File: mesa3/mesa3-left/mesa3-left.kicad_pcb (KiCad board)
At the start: 2 copper layers, 214 x 111 mm, 55 parts, among them J2 Tag-Connect TC2030

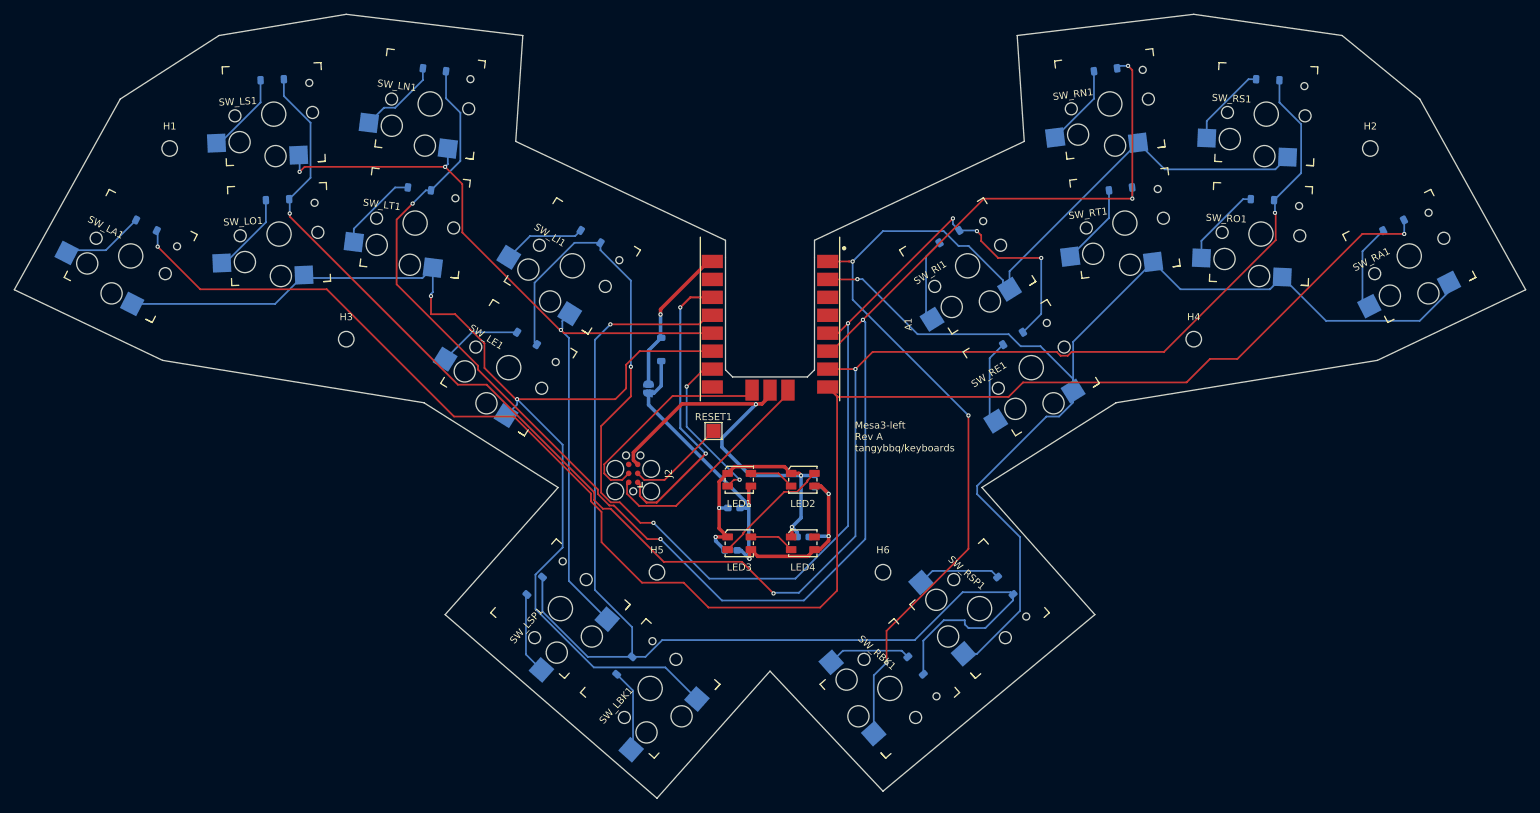
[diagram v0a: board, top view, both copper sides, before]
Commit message: Split the Mesa 3 into left and right halves
Each half now carries its own nine keys, its own outline and its own
routing. The left keeps the Tiny2040, the LEDs, the Tag-Connect and the
reset pad; the right is switches, diodes and the RJ-45 and nothing else,
with no power and no ground anywhere on it.

The two checks that mattered both hold. The RJ-45 pinout is identical at
both ends, so a straight-through cable is correct -- the pin order runs
opposite between the halves, which is what a part that cannot be mirrored
does, and does not matter since the nets match. And all eighteen keys
keep their exact mesa2 column and row, so one keymap still serves Rev B
and both halves.

Record the review findings as accepted rather than outstanding, and
correct LAYOUT.md: the unconnected GND that DRC reports is a false
positive. The symbol ties the module's ground pads into one net, so DRC
wants copper between them, but the module commons them internally and
the board does not need to.

Assisted-by: Claude:opus-5
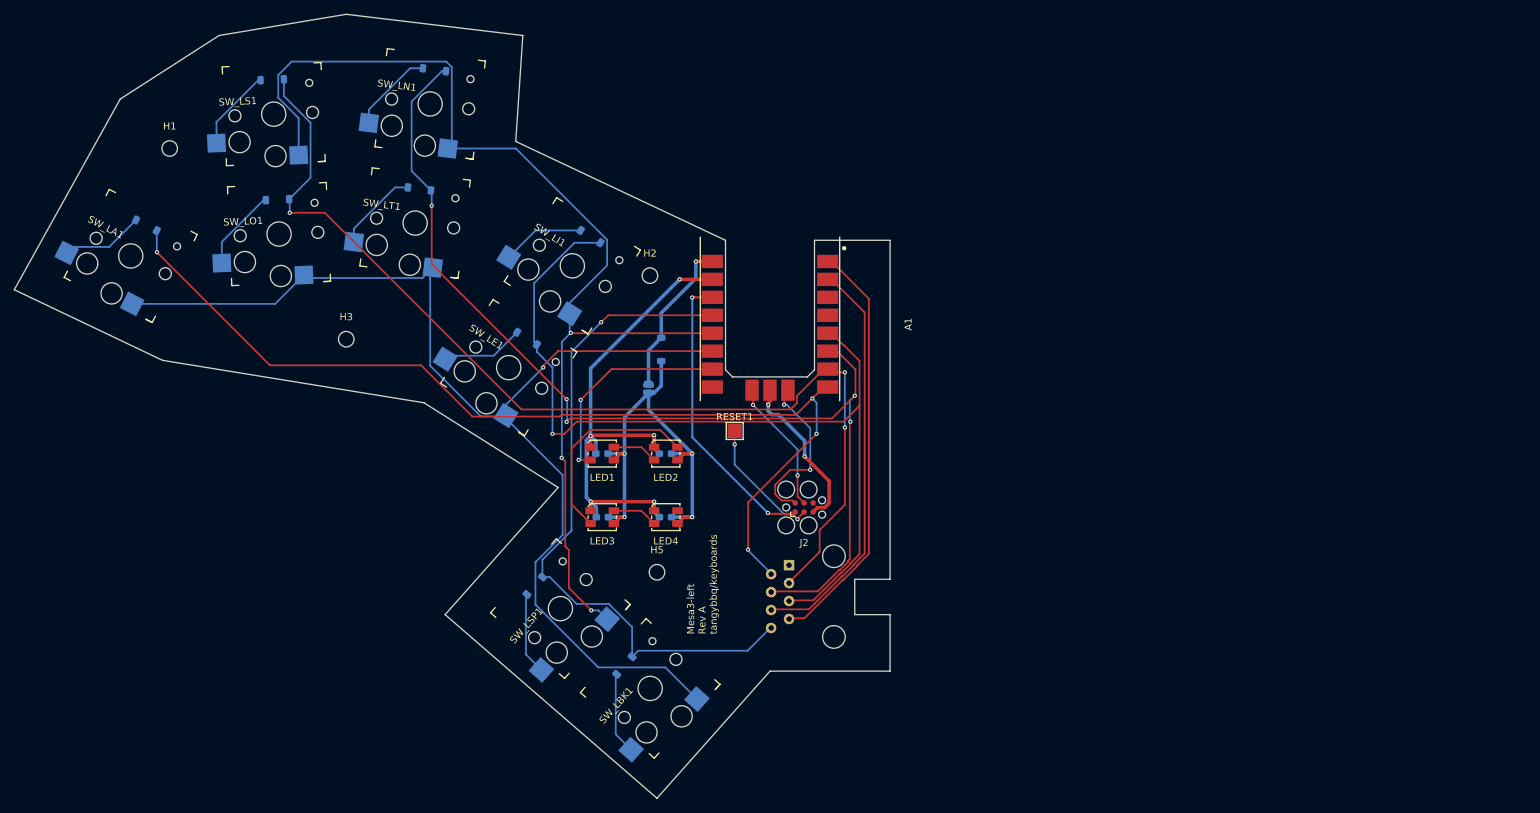
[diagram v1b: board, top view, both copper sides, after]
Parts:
- removed D_RA1, D_RBK1, D_RE1, D_RI1, D_RN1, D_RO1, D_RS1, D_RSP1, D_RT1: 1N4148W, Diode_SMD:D_SOD-123
- removed H4, H6: MountingHole, MountingHole:MountingHole_2.2mm_M2
- removed SW_RA1, SW_RBK1, SW_RE1, SW_RI1, SW_RN1, SW_RO1, SW_RS1, SW_RSP1, SW_RT1: SW_PG1350, mesa1:Kailh_socket_PG1350
- added J1: RJ45, Connector_RJ:RJ45_Amphenol_54602-x08_Horizontal, B.Cu at (137.7, 104.0)
- moved H2 103.6 mm to (118.0, 63.0)
- moved J2 24.7 mm to (139.8, 95.8), turned to 0 degrees
- moved C3 21.4 mm to (120.2, 88.2), turned to 180 degrees
- moved C1 20.2 mm to (111.2, 88.2)
- moved LED1 19.7 mm to (111.2, 88.2)
- moved LED2 19.7 mm to (120.2, 88.2)
- moved LED3 19.7 mm to (111.2, 97.2)
- moved LED4 19.7 mm to (120.2, 97.2)
- moved C4 19.7 mm to (120.2, 97.2)
- moved C2 18.8 mm to (111.3, 97.2)
- moved RESET1 3.00 mm to (130.0, 85.0)
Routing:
- net /ROW_D: track 165.9 -> 57.9 mm, vias 1 -> 0
- net /COL_1: track 247.0 -> 139.9 mm, vias 2 -> 4
- net /ROW_C: track 162.1 -> 59.3 mm, vias 3 -> 0
- net /COL_2: track 249.2 -> 148.2 mm, vias 4 -> 3
- net /COL_3: track 230.0 -> 148.9 mm
- net /COL_5: track 165.2 -> 96.9 mm
- net /COL_4: track 183.1 -> 125.6 mm, vias 6 -> 1
- net /ROW_A: track 124.1 -> 158.0 mm
- net /GND: track 86.0 -> 99.5 mm, vias 5 -> 7
- net Net-(D_RA1-A): track 12.3 -> 0.00 mm
- net Net-(D_RI1-A): track 12.0 -> 0.00 mm
- net Net-(D_RE1-A): track 12.0 -> 0.00 mm
- net Net-(D_RSP1-A): track 11.9 -> 0.00 mm
- net Net-(D_RBK1-A): track 11.9 -> 0.00 mm
- net Net-(LED2-DOUT): track 17.0 -> 28.8 mm
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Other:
- board size 214 x 111 mm -> 124 x 111 mm

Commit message: Bump both mesa3 halves to Rev B
Rev A of both halves has gone to the fab and the boards are on their way
here, so by the rule in mesa3-tasks.md the letter moves on before any
further change is made to the designs.  This commit is the bump alone and
touches no geometry, netlist or routing.

Each half carries the revision in three places, all updated together: the
PCB and schematic title blocks, and sch_revision in the project file.  The
silkscreen legend that the bare board is identified by moves with them, so
the delivered Rev A boards stay distinguishable from whatever Rev B
becomes.

KiCad also reordered used_designators in mesa3-right.kicad_pro while
saving; the set is unchanged.
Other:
- board text added: "Mesa3-left Rev B tangybbq/keyboards"
- board text removed: "Mesa3-left Rev A tangybbq/keyboards"
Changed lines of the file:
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@@
 		(title "mesa3-left")
 		(date "2026-08-09")
-		(rev "A")
+		(rev "B")
 	)
 	(layers
@@
 		(layer "Edge.Cuts")
 	)
-	(gr_text "Mesa3-left\nRev A\ntangybbq/keyboards"
+	(gr_text "Mesa3-left\nRev B\ntangybbq/keyboards"
 		(at 127.6 113.8 90)
 		(layer "F.SilkS")

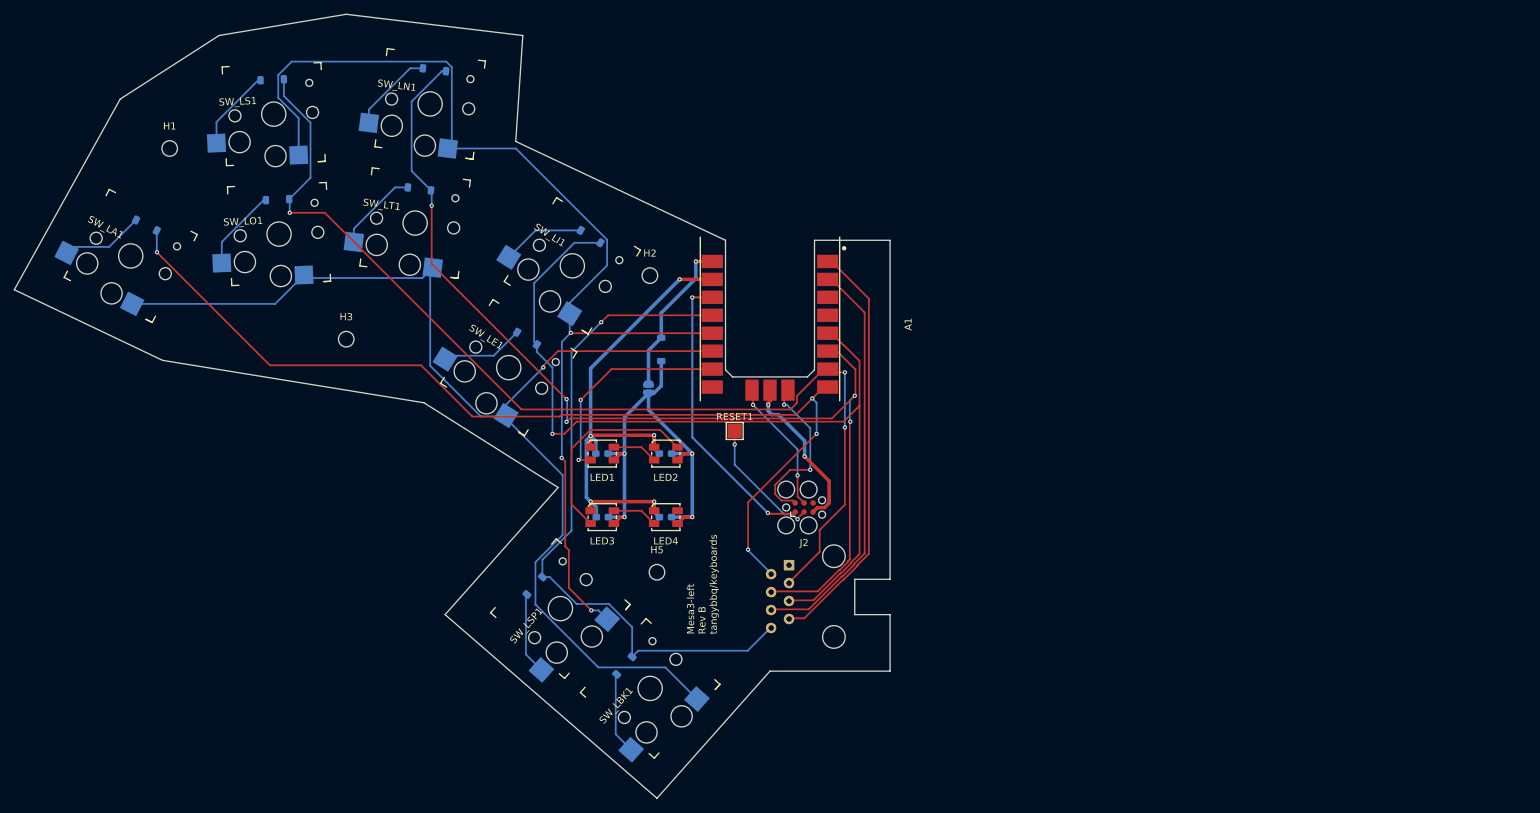
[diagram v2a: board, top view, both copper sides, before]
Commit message: Add the FN mode key to mesa3-left and place it
The Rev B change lands on the left half: SW_LFN1 and D_LFN1, one key
inboard of the near-row index key, for mode switching.  It takes the slot
the dropped outer pinky left free — SW_LFN1 pad 1 on ROW_A, D_LFN1 pad 1
on COL_1 — so it costs no GPIO, and since pinky A sits on ROW_B the two
share COL_1 without colliding.

Placement comes from fnkey.py rather than the mouse.  The key was first
dropped by hand at (112.700, 84.700), which measured 17.053 mm along
SW_LE1's local X with 0.435 mm of lateral drift; the computed position is
(113.272, 85.571) at a clean local (18, 0), a move of 1.042 mm.  D_LFN1
follows at the usual (0, -4.876) offset.  The cap gap against SW_LE1 comes
out at 0.500 mm exactly, which is the board's new worst gap, just inside
the 0.496 mm the thumb pair already had.  LAYOUT.md records both positions
and the rule that produced them.

Two things this commit deliberately contains.  All routing is gone — 308
segments and 41 vias — removed on purpose, to be redone once the non-switch
components settle; the four zones are untouched.  And the support parts
have moved to clear the new key: the four LEDs and their caps, D1, JP1, J2
and the reset pad.  Those are hand-placed and not governed by LAYOUT.md,
which speaks for the keys.

Watch JP1: it clears the new keycap edge by 0.52 mm.  Nothing sits under
the cap or the switch body, but JP1 is the bypass jumper across D1 and an
iron has to reach it.
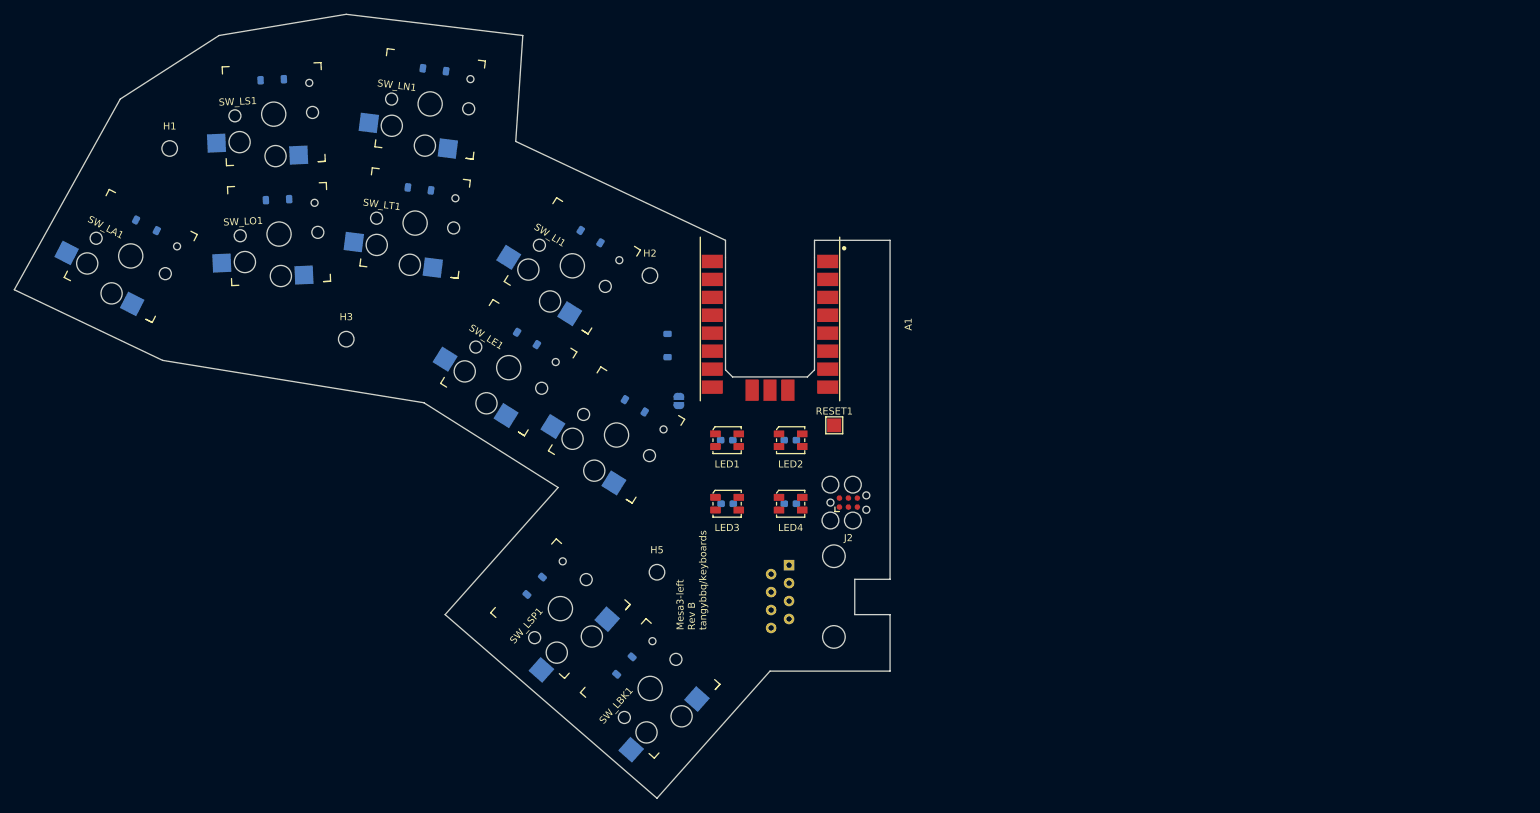
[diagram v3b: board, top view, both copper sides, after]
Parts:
- added D_LFN1: 1N4148W, Diode_SMD:D_SOD-123, B.Cu at (115.9, 81.4)
- added SW_LFN1: SW_PG1350, mesa1:Kailh_socket_PG1350, F.Cu at (113.3, 85.6)
- moved LED1 17.8 mm to (128.9, 86.3)
- moved LED2 17.8 mm to (137.9, 86.3)
- moved LED3 17.8 mm to (128.9, 95.3)
- moved LED4 17.8 mm to (137.9, 95.3)
- moved C1 17.8 mm to (128.9, 86.3)
- moved C2 17.8 mm to (128.9, 95.3)
- moved C3 17.8 mm to (137.9, 86.3)
- moved C4 17.8 mm to (137.9, 95.3)
- moved RESET1 14.1 mm to (144.1, 84.2)
- moved J2 6.30 mm to (146.1, 95.1)
- moved JP1 4.64 mm to (122.1, 80.8)
- moved D1 1.05 mm to (120.5, 72.9)
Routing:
- net /ROW_B: track 167.0 -> 0.00 mm, vias 1 -> 0
- net /ROW_A: track 158.0 -> 0.00 mm, vias 3 -> 0
- net /COL_3: track 148.9 -> 0.00 mm, vias 5 -> 0
- net /COL_2: track 148.2 -> 0.00 mm, vias 3 -> 0
- net /COL_1: track 139.9 -> 0.00 mm, vias 4 -> 0
- net /COL_4: track 125.6 -> 0.00 mm, vias 1 -> 0
- net /GND: track 99.5 -> 0.00 mm, vias 7 -> 0
- net /COL_5: track 96.9 -> 0.00 mm, vias 1 -> 0
- net /+4V5: track 64.0 -> 0.00 mm, vias 4 -> 0
- net /ROW_C: track 59.3 -> 0.00 mm
- net /ROW_D: track 57.9 -> 0.00 mm
- net /+3V3: track 41.8 -> 0.00 mm, vias 2 -> 0
- net /RGB: track 30.8 -> 0.00 mm, vias 2 -> 0
- net Net-(LED2-DOUT): track 28.8 -> 0.00 mm
- net /SWDIO: track 23.8 -> 0.00 mm, vias 2 -> 0
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
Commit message: Route both mesa3 halves and finish the right FN key
Rev B is now routed on both hands.  The left half went from bare
placement to 337 segments and 36 vias; the right went from 118 segments
and 7 vias to 149 and 9 as the mode key was wired in.  That key was the
last thing outstanding — on the right the switch and diode were on the
board but deliberately left disconnected, and they now sit at
COL_1/ROW_C, one of the two slots the dropped outer pinky freed,
matching COL_1/ROW_A on the left.  Each half therefore gains one Kailh
socket and one 1N4148W over Rev A.

fnkey.py now places both halves instead of only the left, as its own
docstring said it should when the right-hand key was still undecided.
Each FN key is derived from its own anchor — a local (PITCH, 0) offset
in SW_xE1's frame, carrying that switch's rotation — and the sign flips
on the right, where local +X points outboard rather than inboard.
Because the two halves are computed independently, their mirror
symmetry is a genuine cross-check rather than a restatement of the same
arithmetic, so the script now makes it one: it refuses to write unless
every switch and diode pair sums to 270.0 mm in x, shares a y, and has
opposite rotations.  The hand placement this replaced was 0.846 mm out;
the new keycap clears SW_RE1 by the 0.500 mm target exactly.

apply-fnkey.py follows, walking both boards from a board-keyed
fn-placement.json and saving only the ones that actually moved.  It
still goes through pcbnew rather than Konnect's IPC path, which
continues to segfault KiCAD 10.0.5 on this machine.

Assisted-by: Claude:opus-5
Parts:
- moved LED1 4.46 mm to (125.5, 89.1)
- moved LED3 4.46 mm to (125.5, 98.1)
- moved C1 4.46 mm to (125.4, 89.1)
- moved C2 4.46 mm to (125.5, 98.1)
- moved C3 4.46 mm to (134.4, 89.1)
- moved C4 4.46 mm to (134.4, 98.1)
- moved LED2 4.46 mm to (134.5, 89.1)
- moved LED4 4.46 mm to (134.5, 98.1)
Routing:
- net /ROW_B: track 0.00 -> 177.8 mm, vias 0 -> 3
- net /COL_2: track 0.00 -> 154.8 mm, vias 0 -> 1
- net /COL_1: track 0.00 -> 148.8 mm, vias 0 -> 2
- net /COL_3: track 0.00 -> 146.4 mm, vias 0 -> 1
- net /ROW_A: track 0.00 -> 124.8 mm, vias 0 -> 3
- net /COL_4: track 0.00 -> 122.9 mm, vias 0 -> 1
- net /COL_5: track 0.00 -> 98.8 mm, vias 0 -> 3
- net /GND: track 0.00 -> 70.3 mm, vias 0 -> 6
- net /+4V5: track 0.00 -> 60.2 mm, vias 0 -> 5
- net /ROW_C: track 0.00 -> 59.7 mm
- net /ROW_D: track 0.00 -> 56.2 mm
- net /+3V3: track 0.00 -> 46.3 mm, vias 0 -> 2
- net /SWCLK: track 0.00 -> 30.6 mm, vias 0 -> 2
- net /+5V: track 0.00 -> 23.7 mm, vias 0 -> 1
- net Net-(LED2-DOUT): track 0.00 -> 20.6 mm
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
